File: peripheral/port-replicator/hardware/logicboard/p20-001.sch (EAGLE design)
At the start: 27 parts, among them IC11 74ALS04N, J0 DC9V, J11 AUDIO_JACK_3.5MM_PTH, J12 AUDIO_JACK_3.5MM_PTH, J13 AUDIO_JACK_3.5MM_PTH, J14 AUDIO_JACK_3.5MM_PTH, J7 DIN5, J8 DIN5, J9 DIN5, X0 MKDSN1,5/2-5,08

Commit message: LED -> L.
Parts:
- renumbered LED0/1 to L0/1, LED2 to L2, LED3 to L3, LED4 to L4
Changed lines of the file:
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@@
 <part name="R11" library="rcl" library_urn="urn:adsk.eagle:library:334" deviceset="R-EU_" device="0204/5" package3d_urn="urn:adsk.eagle:package:23488/1"/>
 <part name="R2" library="rcl" library_urn="urn:adsk.eagle:library:334" deviceset="R-EU_" device="0204/5" package3d_urn="urn:adsk.eagle:package:23488/1"/>
-<part name="LED4" library="led" library_urn="urn:adsk.eagle:library:259" deviceset="LED" device="3MM" package3d_urn="urn:adsk.eagle:package:15797/1" value="PWR"/>
-<part name="LED2" library="led" library_urn="urn:adsk.eagle:library:259" deviceset="LED" device="3MM" package3d_urn="urn:adsk.eagle:package:15797/1" value="IN"/>
-<part name="LED3" library="led" library_urn="urn:adsk.eagle:library:259" deviceset="LED" device="3MM" package3d_urn="urn:adsk.eagle:package:15797/1" value="OUT"/>
+<part name="L4" library="led" library_urn="urn:adsk.eagle:library:259" deviceset="LED" device="3MM" package3d_urn="urn:adsk.eagle:package:15797/1" value="PWR"/>
+<part name="L2" library="led" library_urn="urn:adsk.eagle:library:259" deviceset="LED" device="3MM" package3d_urn="urn:adsk.eagle:package:15797/1" value="IN"/>
+<part name="L3" library="led" library_urn="urn:adsk.eagle:library:259" deviceset="LED" device="3MM" package3d_urn="urn:adsk.eagle:package:15797/1" value="OUT"/>
 <part name="R3" library="rcl" library_urn="urn:adsk.eagle:library:334" deviceset="R-EU_" device="0204/5" package3d_urn="urn:adsk.eagle:package:23488/1"/>
 <part name="SUPPLY1" library="supply2" deviceset="GND" device=""/>
@@
 <part name="S1" library="switch-omron" library_urn="urn:adsk.eagle:library:377" deviceset="10-XX" device="" package3d_urn="urn:adsk.eagle:package:27496/1"/>
 <part name="JP6" library="pinhead" library_urn="urn:adsk.eagle:library:325" deviceset="PINHD-1X3" device="" package3d_urn="urn:adsk.eagle:package:22458/2"/>
-<part name="LED0/1" library="led" library_urn="urn:adsk.eagle:library:259" deviceset="DUOLED-RG-C" device="" package3d_urn="urn:adsk.eagle:package:15851/1"/>
+<part name="L0/1" library="led" library_urn="urn:adsk.eagle:library:259" deviceset="DUOLED-RG-C" device="" package3d_urn="urn:adsk.eagle:package:15851/1"/>
 <part name="RN1" library="resistor-net" library_urn="urn:adsk.eagle:library:343" deviceset="RN04" device="" package3d_urn="urn:adsk.eagle:package:24976/1"/>
 <part name="SUPPLY2" library="supply2" deviceset="GND" device=""/>
@@
 <attribute name="VALUE" x="255.27" y="154.178" size="1.778" layer="96"/>
 </instance>
-<instance part="LED4" gate="G$1" x="35.56" y="167.64" smashed="yes">
+<instance part="L4" gate="G$1" x="35.56" y="167.64" smashed="yes">
 <attribute name="NAME" x="39.116" y="163.068" size="1.778" layer="95" rot="R90"/>
 <attribute name="VALUE" x="41.275" y="163.068" size="1.778" layer="96" rot="R90"/>
 </instance>
-<instance part="LED2" gate="G$1" x="271.78" y="157.48" smashed="yes" rot="R270">
+<instance part="L2" gate="G$1" x="271.78" y="157.48" smashed="yes" rot="R270">
 <attribute name="NAME" x="267.208" y="153.924" size="1.778" layer="95"/>
 <attribute name="VALUE" x="267.208" y="151.765" size="1.778" layer="96"/>
 </instance>
-<instance part="LED3" gate="G$1" x="271.78" y="139.7" smashed="yes" rot="R270">
+<instance part="L3" gate="G$1" x="271.78" y="139.7" smashed="yes" rot="R270">
 <attribute name="NAME" x="267.208" y="136.144" size="1.778" layer="95"/>
 <attribute name="VALUE" x="267.208" y="133.985" size="1.778" layer="96"/>
@@
 <attribute name="VALUE" x="39.37" y="45.72" size="1.778" layer="96" rot="MR0"/>
 </instance>
-<instance part="LED0/1" gate="G$1" x="58.42" y="170.18" smashed="yes">
+<instance part="L0/1" gate="G$1" x="58.42" y="170.18" smashed="yes">
 <attribute name="NAME" x="64.77" y="165.1" size="1.778" layer="95" rot="R90"/>
 <attribute name="VALUE" x="67.31" y="165.1" size="1.778" layer="96" rot="R90"/>
@@
 </segment>
 <segment>
-<pinref part="LED4" gate="G$1" pin="C"/>
+<pinref part="L4" gate="G$1" pin="C"/>
 <wire x1="35.56" y1="162.56" x2="35.56" y2="160.02" width="0.1524" layer="91"/>
 <label x="35.56" y="160.02" size="0.8128" layer="95" rot="R270" xref="yes"/>
@@
 </segment>
 <segment>
-<pinref part="LED0/1" gate="G$1" pin="C"/>
+<pinref part="L0/1" gate="G$1" pin="C"/>
 <wire x1="55.88" y1="170.18" x2="53.34" y2="170.18" width="0.1524" layer="91"/>
 <label x="53.34" y="170.18" size="0.8128" layer="95" rot="R180" xref="yes"/>
@@
 </segment>
 <segment>
-<pinref part="LED2" gate="G$1" pin="A"/>
+<pinref part="L2" gate="G$1" pin="A"/>
 <wire x1="279.4" y1="157.48" x2="276.86" y2="157.48" width="0.1524" layer="91"/>
-<pinref part="LED3" gate="G$1" pin="A"/>
+<pinref part="L3" gate="G$1" pin="A"/>
 <wire x1="276.86" y1="157.48" x2="274.32" y2="157.48" width="0.1524" layer="91"/>
 <wire x1="274.32" y1="139.7" x2="276.86" y2="139.7" width="0.1524" layer="91"/>
@@
 <net name="LEDMI" class="0">
 <segment>
-<pinref part="LED2" gate="G$1" pin="C"/>
+<pinref part="L2" gate="G$1" pin="C"/>
 <pinref part="R2" gate="G$1" pin="2"/>
 <wire x1="266.7" y1="157.48" x2="264.16" y2="157.48" width="0.1524" layer="91"/>
@@
 <net name="LEDMO" class="0">
 <segment>
-<pinref part="LED3" gate="G$1" pin="C"/>
+<pinref part="L3" gate="G$1" pin="C"/>
 <pinref part="R3" gate="G$1" pin="2"/>
 <wire x1="266.7" y1="139.7" x2="264.16" y2="139.7" width="0.1524" layer="91"/>
@@
 <segment>
 <pinref part="R11" gate="G$1" pin="1"/>
-<pinref part="LED4" gate="G$1" pin="A"/>
+<pinref part="L4" gate="G$1" pin="A"/>
 <wire x1="35.56" y1="172.72" x2="35.56" y2="170.18" width="0.1524" layer="91"/>
 </segment>
@@
 <net name="LED0" class="0">
 <segment>
-<pinref part="LED0/1" gate="G$1" pin="AR"/>
+<pinref part="L0/1" gate="G$1" pin="AR"/>
 <wire x1="58.42" y1="177.8" x2="58.42" y2="180.34" width="0.1524" layer="91"/>
 <label x="58.42" y="180.34" size="0.8128" layer="95" rot="R90" xref="yes"/>
@@
 <net name="LED1" class="0">
 <segment>
-<pinref part="LED0/1" gate="G$1" pin="AG"/>
+<pinref part="L0/1" gate="G$1" pin="AG"/>
 <wire x1="58.42" y1="162.56" x2="58.42" y2="160.02" width="0.1524" layer="91"/>
 <label x="58.42" y="160.02" size="0.8128" layer="95" rot="R270" xref="yes"/>

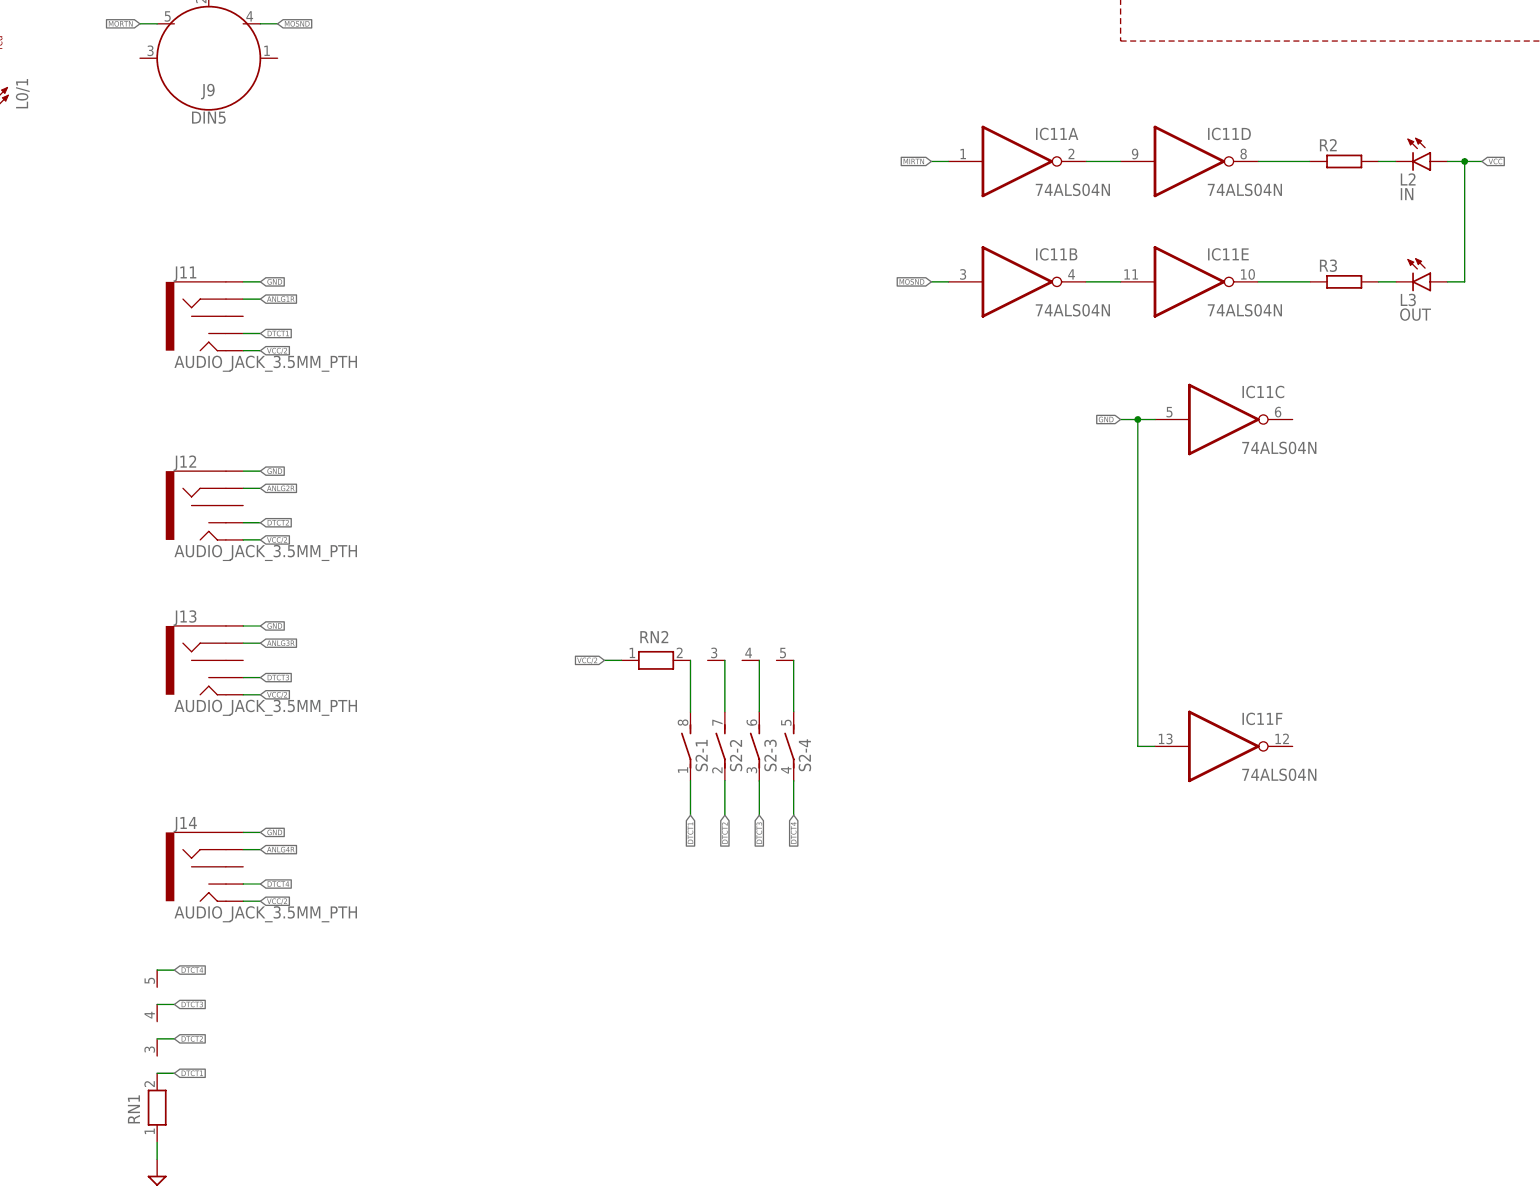
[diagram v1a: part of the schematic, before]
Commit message: Fixed DTCT circuits.
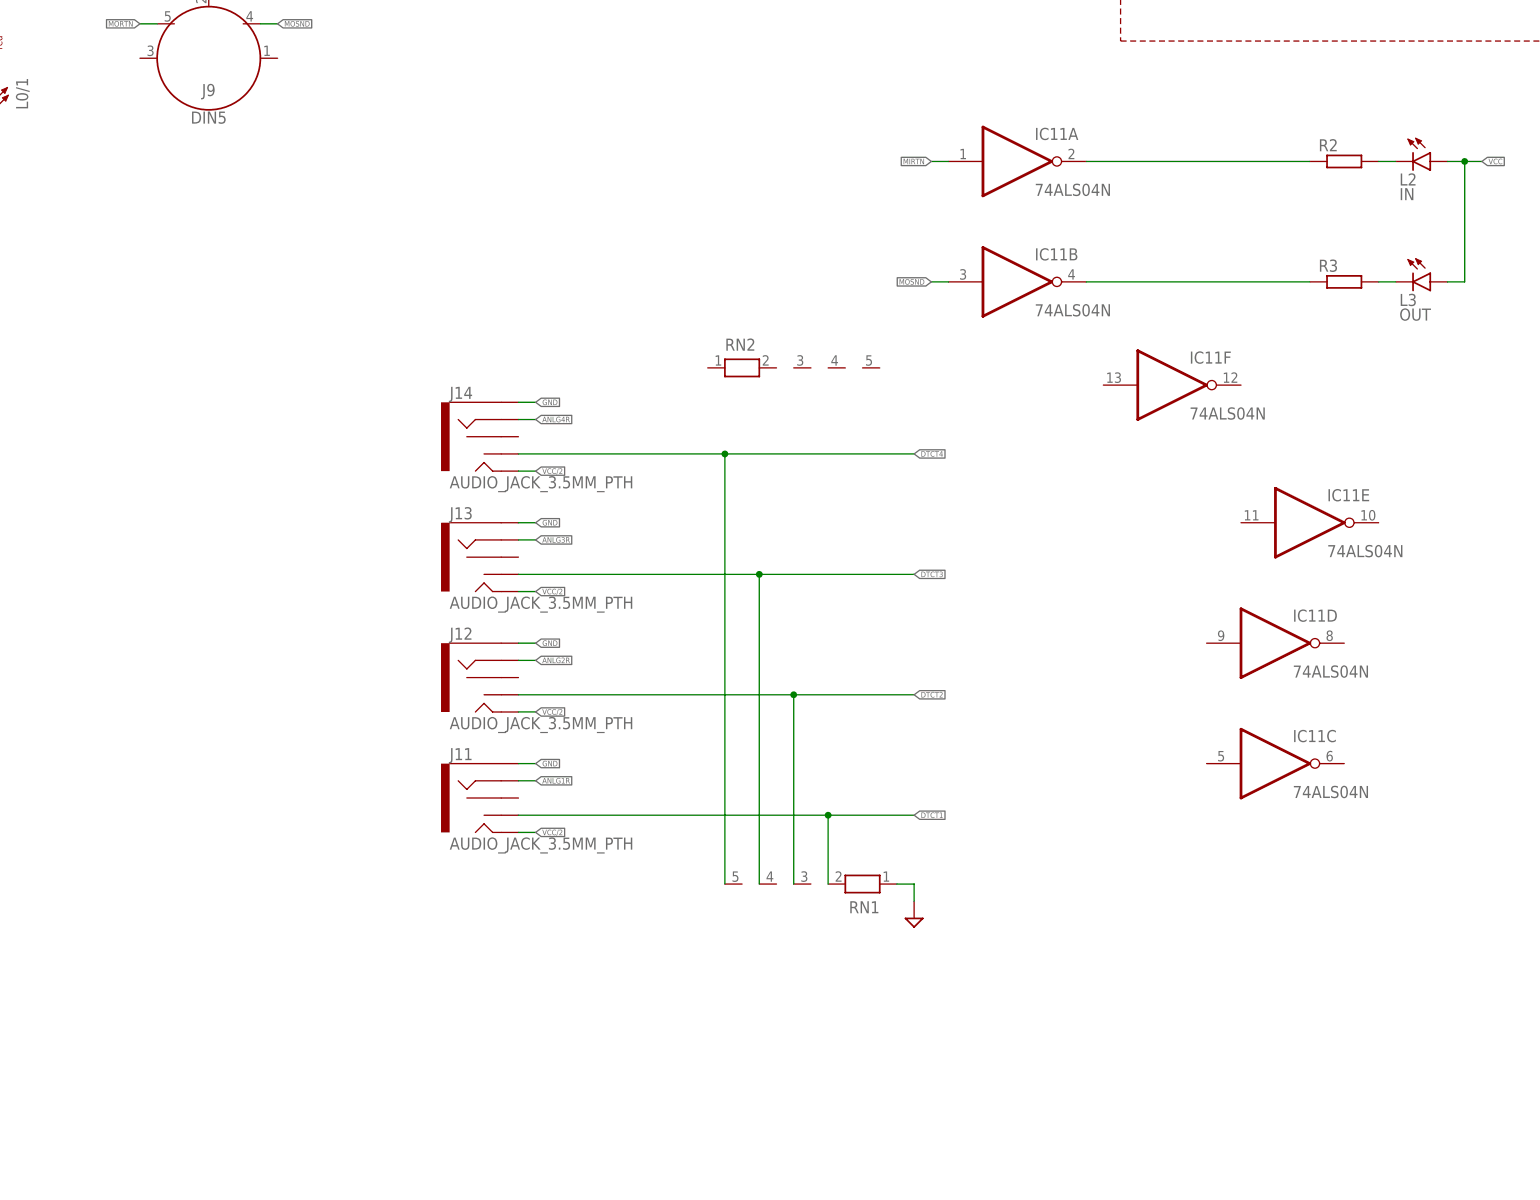
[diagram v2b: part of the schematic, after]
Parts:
- removed S2: (no value), switch-dil:DIP04S
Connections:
- removed net N$3: IC11D.O, R2.1
- removed net N$4: IC11E.O, R3.1
- removed net N$5: RN2.2, S2-1.2
- removed net N$6: RN2.3, S2-2.2
- removed net N$7: RN2.4, S2-3.2
- removed net N$8: RN2.5, S2-4.2
- net DTCT1: no longer S2-1.1
- net DTCT2: no longer S2-2.1
- net DTCT3: no longer S2-3.1
- net DTCT4: no longer S2-4.1
- net GND: no longer IC11C.I, IC11F.I
- net N$1: now also R2.1; no longer IC11D.I
- net N$2: now also R3.1; no longer IC11E.I
- net VCC/2: no longer RN2.1
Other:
- moved on the sheet: IC11C, IC11D, IC11E, IC11F, J11, J12, J13, J14, RN1, RN2

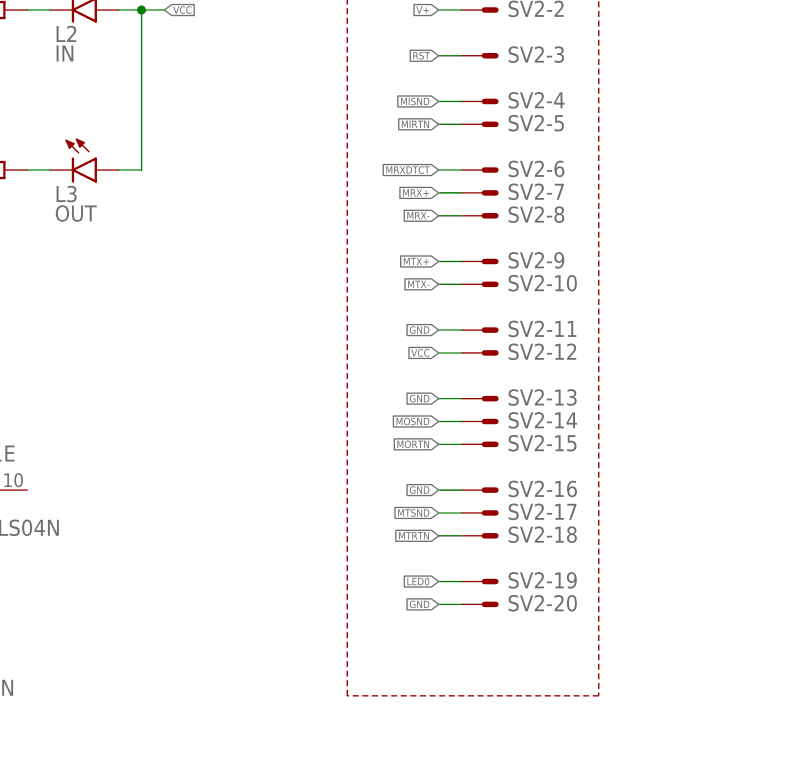
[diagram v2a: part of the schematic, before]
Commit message: Updated backport pintouts of port rep.
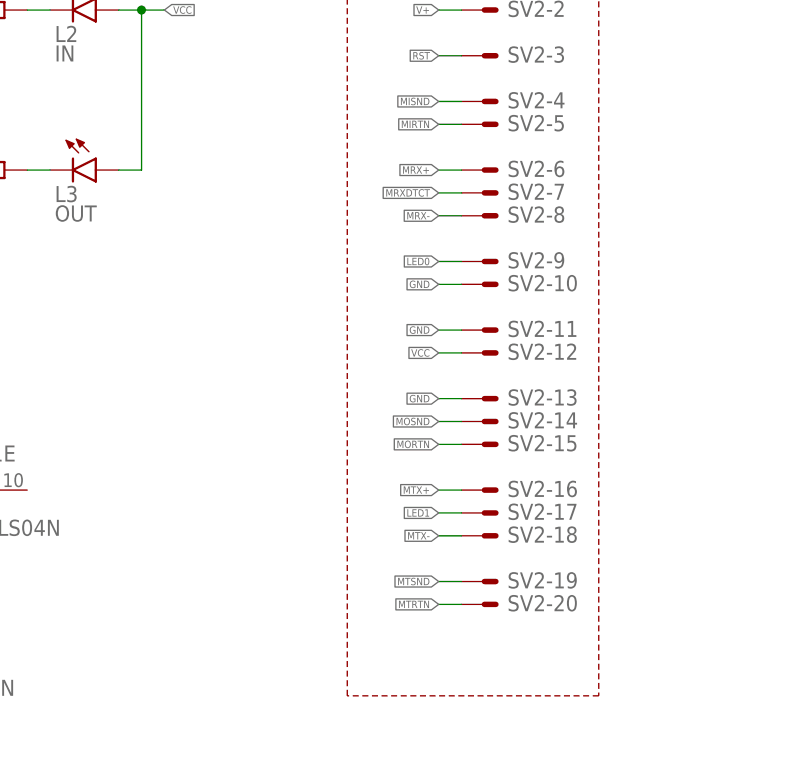
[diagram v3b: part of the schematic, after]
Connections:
- net GND: now also SV2-10.S; no longer SV2-16.S, SV2-20.S
- net LED0: now also SV2-9.S; no longer SV2-19.S
- net LED1: now also SV2-17.S
- net MRX+: now also SV2-6.S; no longer SV2-7.S
- net MRXDTCT: now also SV2-7.S; no longer SV2-6.S
- net MTRTN: now also SV2-20.S; no longer SV2-18.S
- net MTSND: now also SV2-19.S; no longer SV2-17.S
- net MTX+: now also SV2-16.S; no longer SV2-9.S
- net MTX-: now also SV2-18.S; no longer SV2-10.S
